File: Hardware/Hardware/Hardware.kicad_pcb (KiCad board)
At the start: 2 copper layers, 20 x 40 mm, 44 parts, among them J1 TYPE-C-31-M-12, Q1 MMUN2112LT1G, U1 AZ1117CH-3.3TRG1, U2 USBLC6-2SC6, U3 STM32F303CCT6, U4 BMA253, Y1 8Mhz 10pf

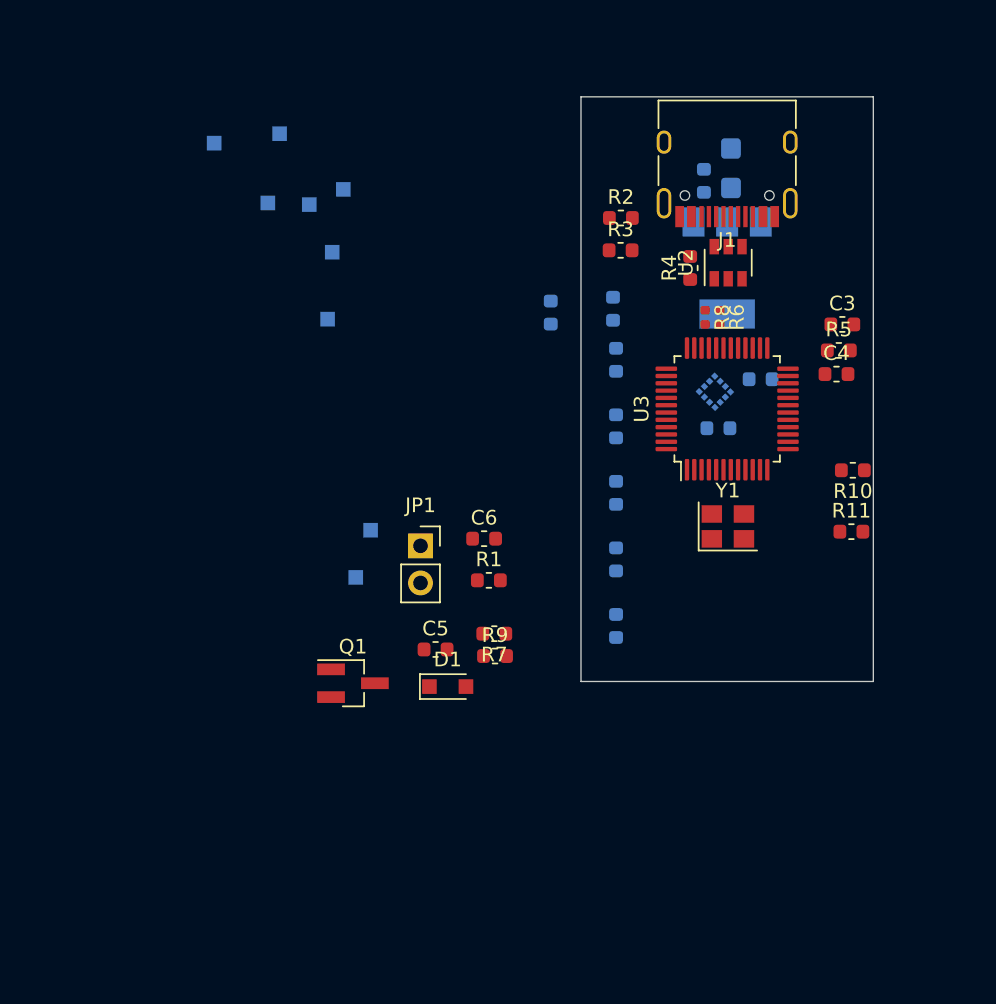
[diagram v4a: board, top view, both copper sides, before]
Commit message: Change to 4 layer board
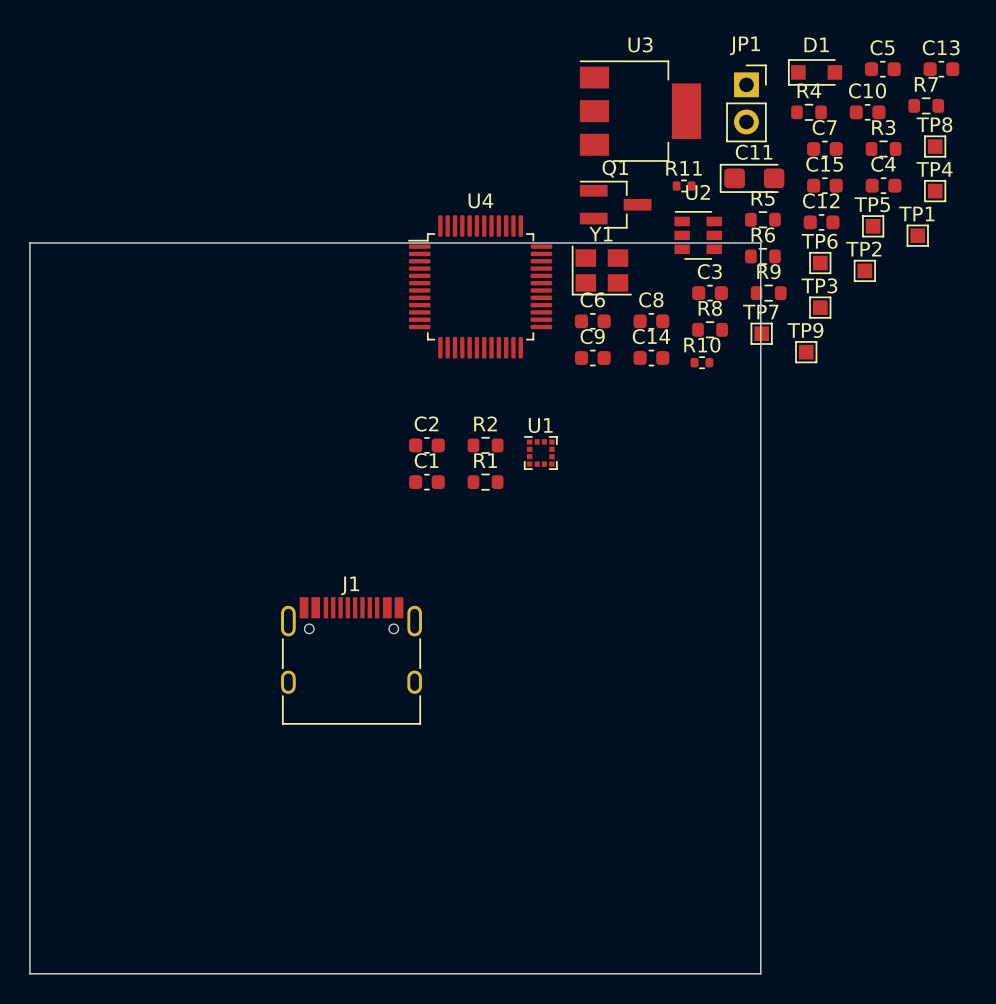
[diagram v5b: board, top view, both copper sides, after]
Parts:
- C1: value 10uf -> 100nF; moved to F.Cu
- C10, C7, C9, TP1, TP2, TP3, TP4, TP5, TP6, TP7, TP8, TP9: moved to F.Cu
- C11: value 4.7uf -> 22uf/10v; footprint Capacitor_SMD:C_0603_1608Metric -> Capacitor_Tantalum_SMD:CP_EIA-3216-18_Kemet-A; moved to F.Cu
- C12: value 10nF -> 100nF; moved to F.Cu
- C13: value 1uf -> 4.7uf; moved to F.Cu
- C14: value 100nF -> 10nF; moved to F.Cu
- C15: value 100nF -> 1uf; moved to F.Cu
- C2: value 22uf/10v -> 100nF; footprint Capacitor_Tantalum_SMD:CP_EIA-3216-18_Kemet-A -> Capacitor_SMD:C_0603_1608Metric; moved to F.Cu
- C8: value 100nF -> 10uf; moved to F.Cu
- R1: value 100k -> 1.5k
- R10, R11: value 1.5k -> 22; footprint Resistor_SMD:R_0603_1608Metric -> Resistor_SMD:R_0402_1005Metric
- R2, R3: value 56k -> 1.5k
- R4: value 1.5k -> 47k
- R5: value 1.5k -> 4.7k
- R6: value 22 -> 100k; footprint Resistor_SMD:R_0402_1005Metric -> Resistor_SMD:R_0603_1608Metric
- R7: value 4.7k -> 56k
- R8: value 22 -> 56k; footprint Resistor_SMD:R_0402_1005Metric -> Resistor_SMD:R_0603_1608Metric
- R9: value 47k -> 1.5k
- U1: value AZ1117CH-3.3TRG1 -> BMA253; footprint Package_TO_SOT_SMD:SOT-223-3_TabPin2 -> Package_LGA:LGA-12_2x2mm_P0.5mm; moved to F.Cu
- U3: value STM32F303CCT6 -> AZ1117CH-3.3TRG1; footprint Package_QFP:LQFP-48_7x7mm_P0.5mm -> Package_TO_SOT_SMD:SOT-223-3_TabPin2
- U4: value BMA253 -> STM32F303CCT6; footprint Package_LGA:LGA-12_2x2mm_P0.5mm -> Package_QFP:LQFP-48_7x7mm_P0.5mm; moved to F.Cu
- moved C5 50.1 mm to (168.3, 58.1)
- moved D1 49.0 mm to (163.8, 58.3)
- moved R7 46.7 mm to (171.3, 60.6), turned to 0 degrees
- moved TP2 45.4 mm to (167.1, 71.9)
- moved TP4 45.0 mm to (171.9, 66.5)
- moved TP1 44.5 mm to (170.7, 69.5)
- moved J1 43.3 mm to (132.0, 99.0), turned to 0 degrees
- moved TP5 42.8 mm to (167.7, 68.9)
- moved TP8 40.6 mm to (171.9, 63.4)
- moved C10 39.1 mm to (167.3, 61.1), turned to 0 degrees
- moved JP1 38.6 mm to (159.0, 59.2)
- moved Q1 37.3 mm to (150.1, 67.4)
- moved C13 36.5 mm to (172.4, 58.1), turned to 0 degrees
- moved TP6 35.8 mm to (164.1, 71.4)
- moved TP3 35.7 mm to (164.1, 74.4)
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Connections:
- C1 pad 1: +5V -> +3V3
- C8 pad 1: +3V3 -> +5V
- J1 pad A8: (no net) -> Net-(J1-PadA8)
- J1 pad B8: (no net) -> Net-(J1-PadB8)
- R1 pad 1: /MCU/BOOT0 -> +3V3
- R1 pad 2: GND -> /SCL
- R10 pad 1: +3V3 -> /MCU/USB_D+
- R10 pad 2: /SCL -> /MCU/D+
- R11 pad 1: +3V3 -> /MCU/USB_D-
- R11 pad 2: /SDA -> /MCU/D-
- R2 pad 1: /MCU/CC1 -> +3V3
- R2 pad 2: +5V -> /SDA
- R3 pad 1: /MCU/CC2 -> /MCU/OSC_OUT
- R3 pad 2: +5V -> Net-(C4-Pad2)
- R4 pad 1: /MCU/USB_D+ -> Net-(Q1-Pad1)
- R4 pad 2: +3V3 -> GND
- R5 pad 1: /MCU/OSC_OUT -> Net-(D1-Pad2)
- R5 pad 2: Net-(C4-Pad2) -> Net-(Q1-Pad1)
- R6 pad 1: /MCU/USB_D- -> /MCU/BOOT0
- R6 pad 2: /MCU/D- -> GND
- R7 pad 1: Net-(D1-Pad2) -> /MCU/CC1
- R7 pad 2: Net-(Q1-Pad1) -> +5V
- R8 pad 1: /MCU/USB_D+ -> /MCU/CC2
- R8 pad 2: /MCU/D+ -> +5V
- R9 pad 1: Net-(Q1-Pad1) -> /MCU/USB_D+
- R9 pad 2: GND -> +3V3
- TP2 pad 1: /MCU/USB_D- -> /MCU/NRST
- TP3 pad 1: +5V -> /SDA
- TP4 pad 1: +3V3 -> /MCU/USB_D-
- TP5 pad 1: /MCU/NRST -> /MCU/BOOT0
- TP6 pad 1: /MCU/BOOT0 -> +3V3
- TP7 pad 1: GND -> +5V
- TP8 pad 1: /SCL -> GND
- TP9 pad 1: /SDA -> /SCL
- U1 pad 2: +3V3 -> /SDA
- U1 pad 3: +5V -> +3V3
- U3 pad 1: +3V3 -> GND
- U3 pad 2: (no net) -> +3V3
- U3 pad 3: (no net) -> +5V
- U4 pad 1: GND -> +3V3
- U4 pad 10: (no net) -> /MCU/PA0
- U4 pad 11: +3V3 -> /MCU/PA1
- U4 pad 12: /SCL -> /MCU/PA2
- U4 pad 2: /SDA -> /MCU/PC13
- U4 pad 3: +3V3 -> /MCU/PC14
- U4 pad 4: GND -> /MCU/PC15
- U4 pad 5: (no net) -> /MCU/OSC_IN
- U4 pad 6: (no net) -> /MCU/OSC_OUT
- U4 pad 7: +3V3 -> /MCU/NRST
- U4 pad 9: GND -> +3V3
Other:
- board size 20 x 40 mm -> 50 x 50 mm
- copper layers 2 -> 4
- net class Clock added: clearance 0.2, trace_width 0.25, via_dia 0.8, via_drill 0.4
- net class Digital added: clearance 0.2, trace_width 0.25, via_dia 0.8, via_drill 0.4
- net class GND added: clearance 0.2, trace_width 0.25, via_dia 0.8, via_drill 0.4
- net class Power added: clearance 0.2, trace_width 0.25, via_dia 0.8, via_drill 0.4
- net class USB added: clearance 0.2, trace_width 0.25, via_dia 0.8, via_drill 0.4
